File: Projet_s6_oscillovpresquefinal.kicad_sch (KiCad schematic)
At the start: 20 parts, among them IC1 PGA849RGTR, J1 Conn_Coaxial, J2 Conn_01x06_Socket, J3 PILES_3AA, SW1 SW_SPST, U1 STM32L476RGTx, U2 MCP6001-OT, U3 AP2112K-3.3, U3 MCP1640x-xCHY

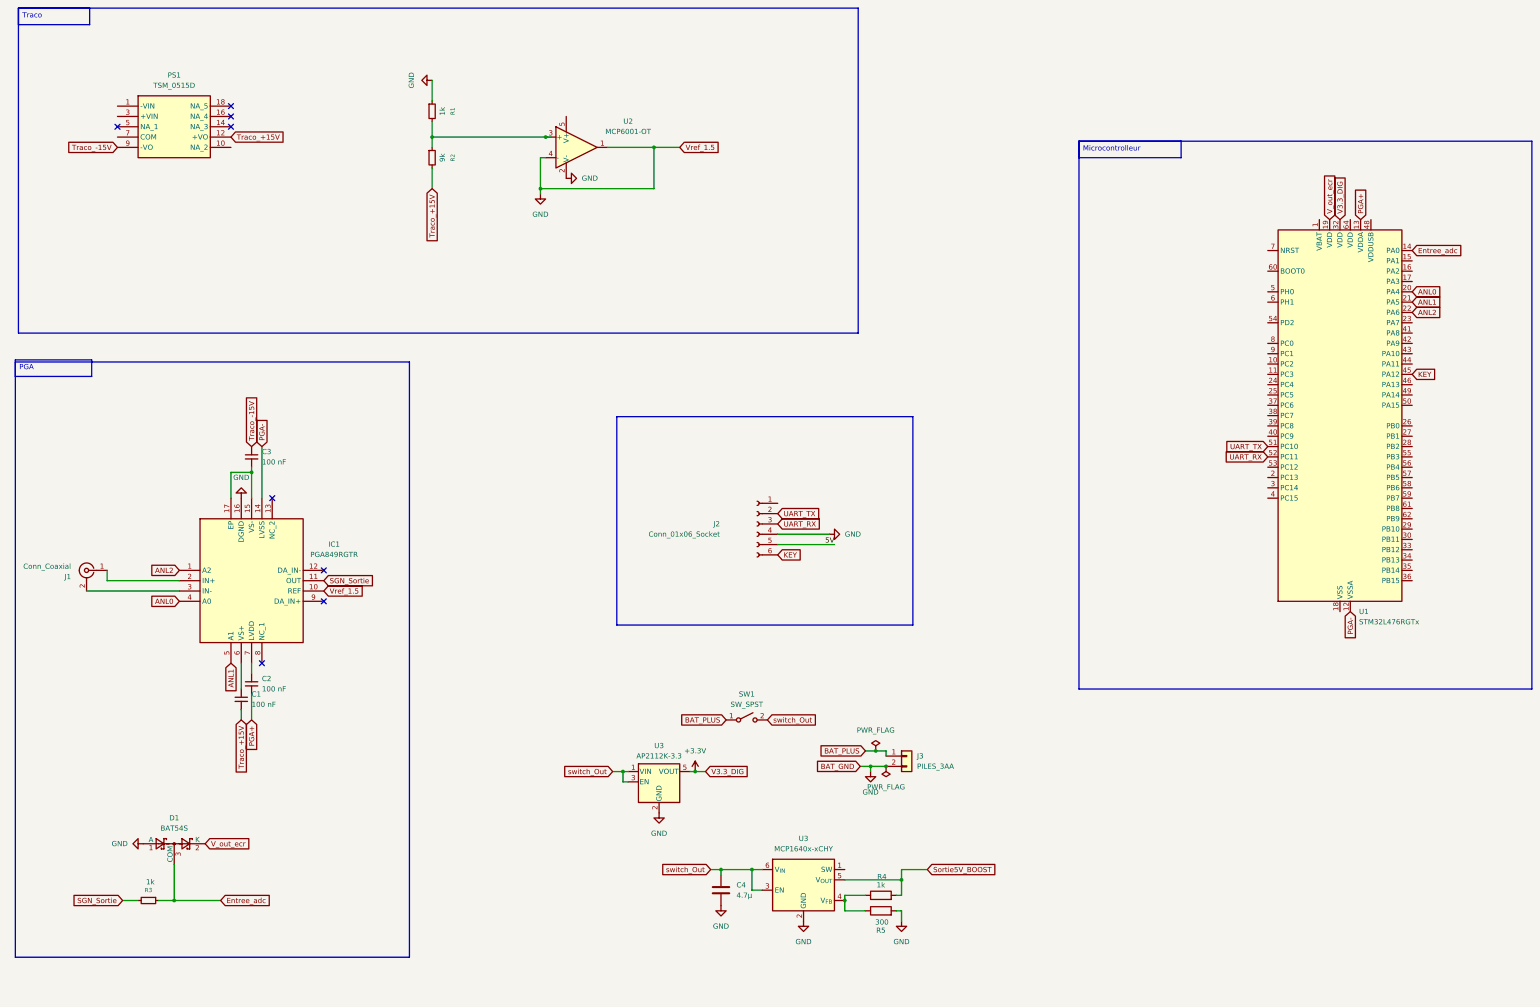
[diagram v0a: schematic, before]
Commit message: Ajout du connecteur SWD et des fixations
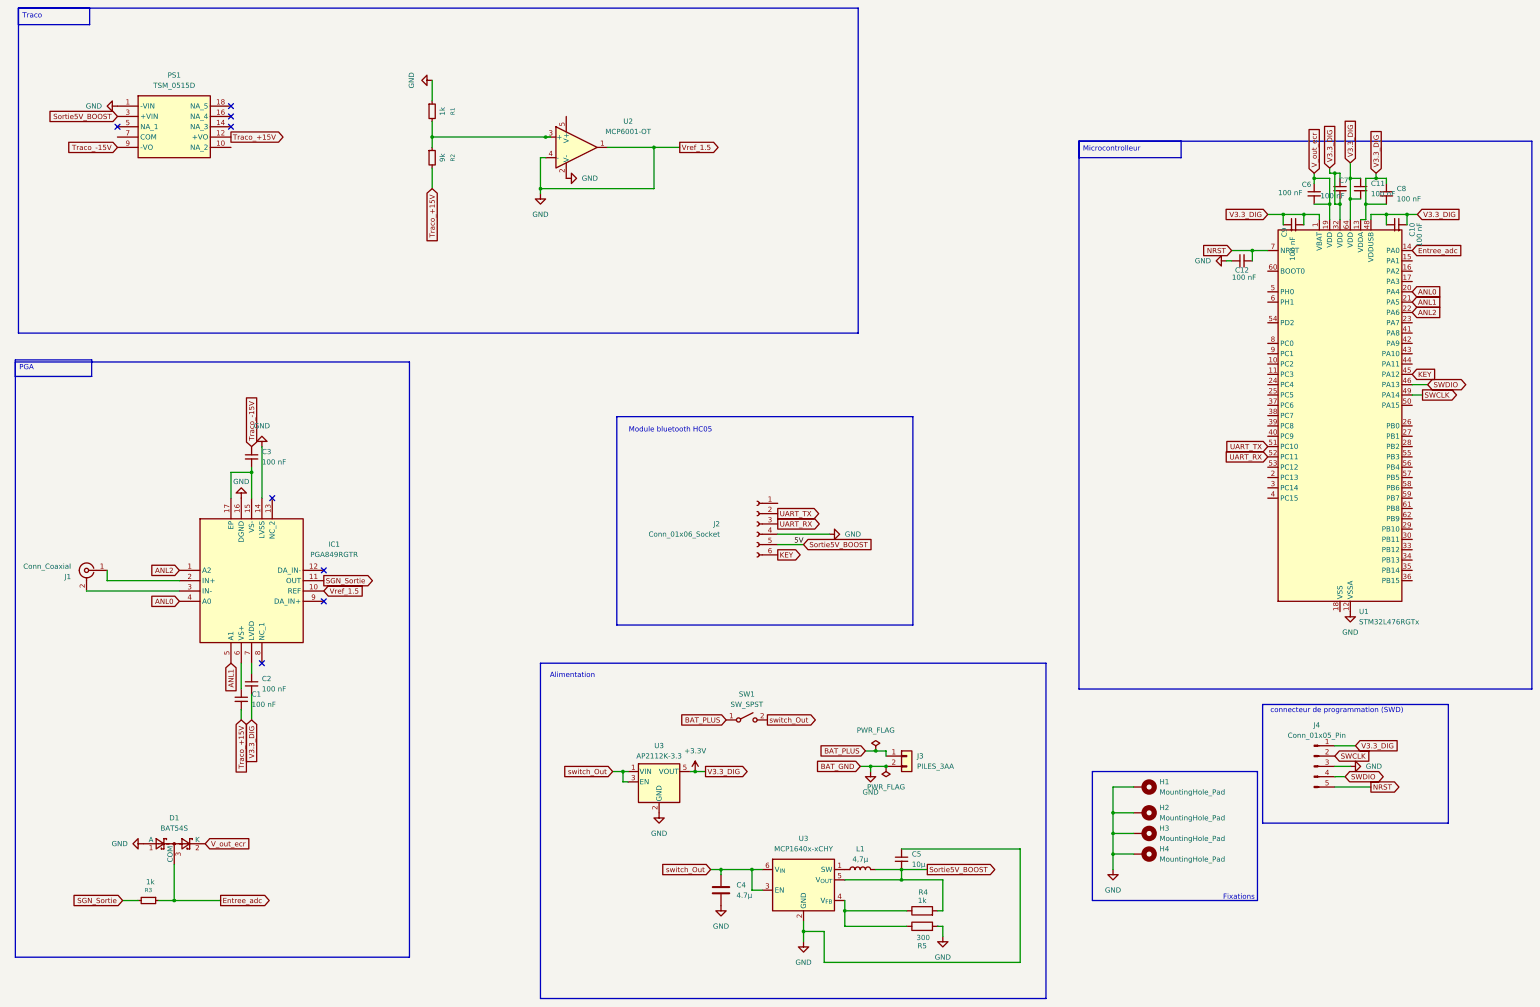
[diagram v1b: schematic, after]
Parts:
- added C10, C11, C12, C6, C7, C8, C9: 100 nF, symbol Device:C_Small
- added C5: 10µ, symbol Device:C_Small
- added H1, H2, H3, H4: MountingHole_Pad, symbol Mechanical:MountingHole_Pad
- added J4: Conn_01x05_Pin, symbol Connector:Conn_01x05_Pin
- added L1: 4,7µ, symbol Device:L
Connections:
- net 5V is gone; now on net Sortie5V_BOOST: J2.5 (Pin_5)
- net PGA+ is gone; now on net +3.3V: C2.2, U1.13 (VDDA)
- net PGA- is gone; now on net GND: IC1.14 (LVSS), U1.12 (VSSA)
- net +3.3V: now also U1.1 (VBAT), U1.48 (VDDUSB), U1.64 (VDD), C10.1, C10.2, C11.1, C11.2, C7.1, C7.2, C8.1, C8.2, C9.1, C9.2, J4.1 (Pin_1)
- net GND: now also PS1.1 (-VIN), C12.1, C5.1, H1.1, H2.1, H3.1, H4.1, J4.3 (Pin_3)
- net Sortie5V_BOOST: now also PS1.3 (+VIN), C5.2, L1.2
- net V_out_ecr: now also C6.1, C6.2
- net SWDIO: now reaches U1.46 (PA13)
- net SWDIO: now also J4.4 (Pin_4)
- net SWCLK: now reaches U1.49 (PA14)
- net SWCLK: now also J4.2 (Pin_2)
- net NRST: now reaches U1.7 (NRST)
- net NRST: now also C12.2, J4.5 (Pin_5)
- net at U3.1 (SW): now also L1.1
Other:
- note added: "Alimentation"
- note added: "Fixations"
- note added: "Module bluetooth HC05"
- note added: "connecteur de programmation (SWD)"
- moved on the sheet: R4, R5
